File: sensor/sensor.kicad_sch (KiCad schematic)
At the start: 29 parts, among them IC1 MAX30002CWV+, IC2 LP5900TLX-2.7_NOPB, IC3 MAX86141ENP+T, J1 Conn_01x10_Female, J2 Conn_01x10_Female, J2 Probe_01_male, J3 Probe_01_male, J4 Probe_01_male, J5 Probe_01_male

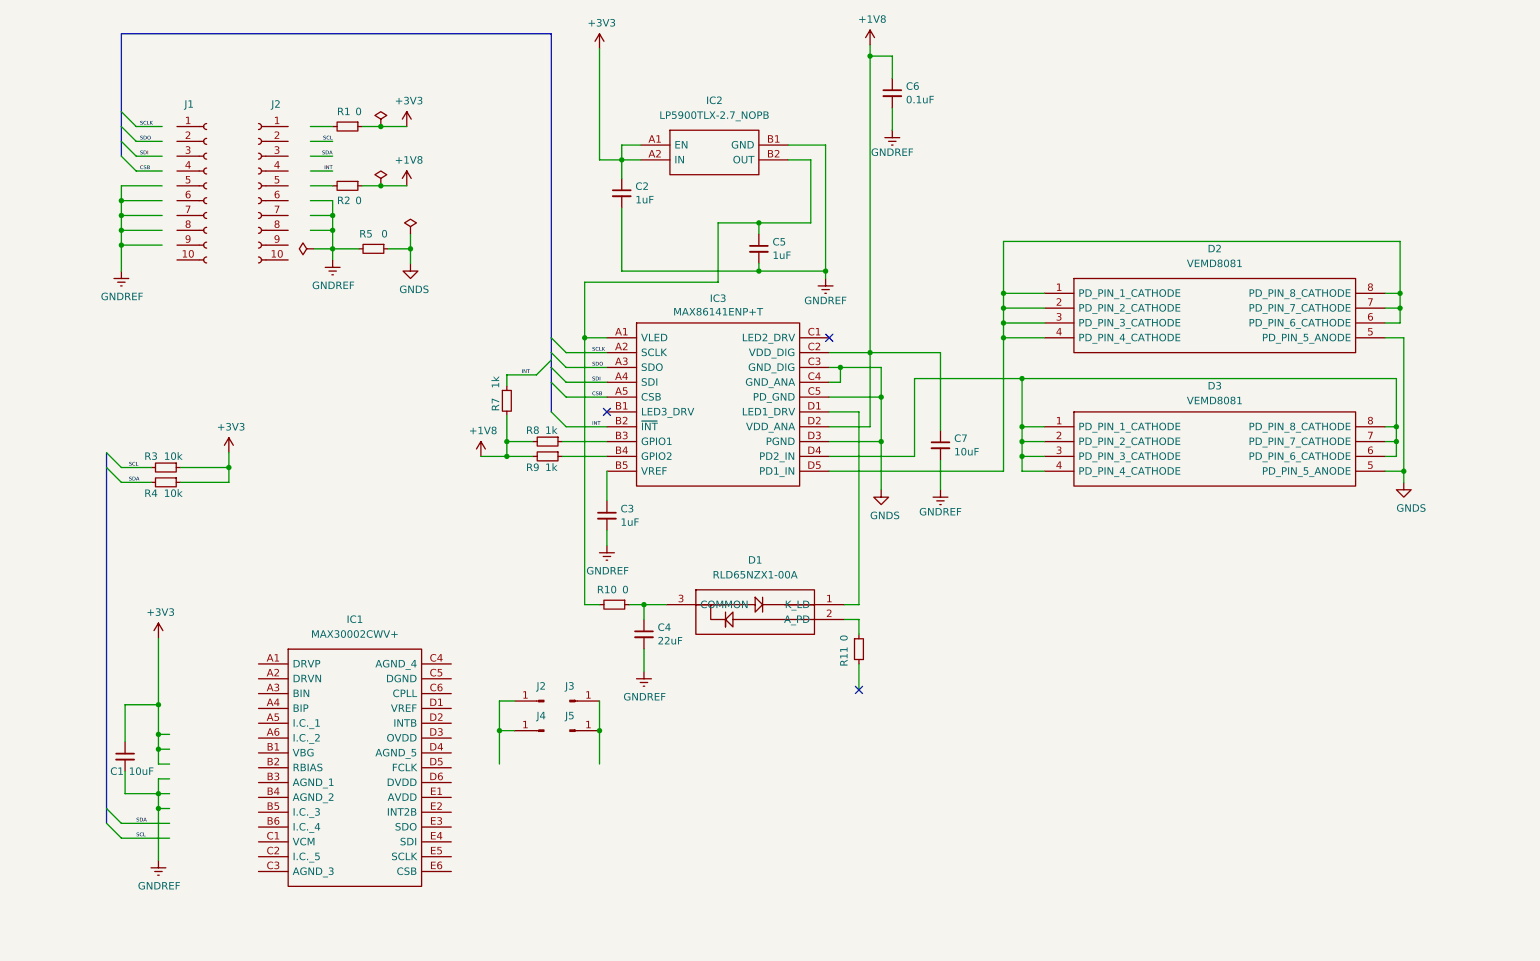
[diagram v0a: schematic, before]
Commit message: Schematic v 2.0 is ready. Can go with PCB design
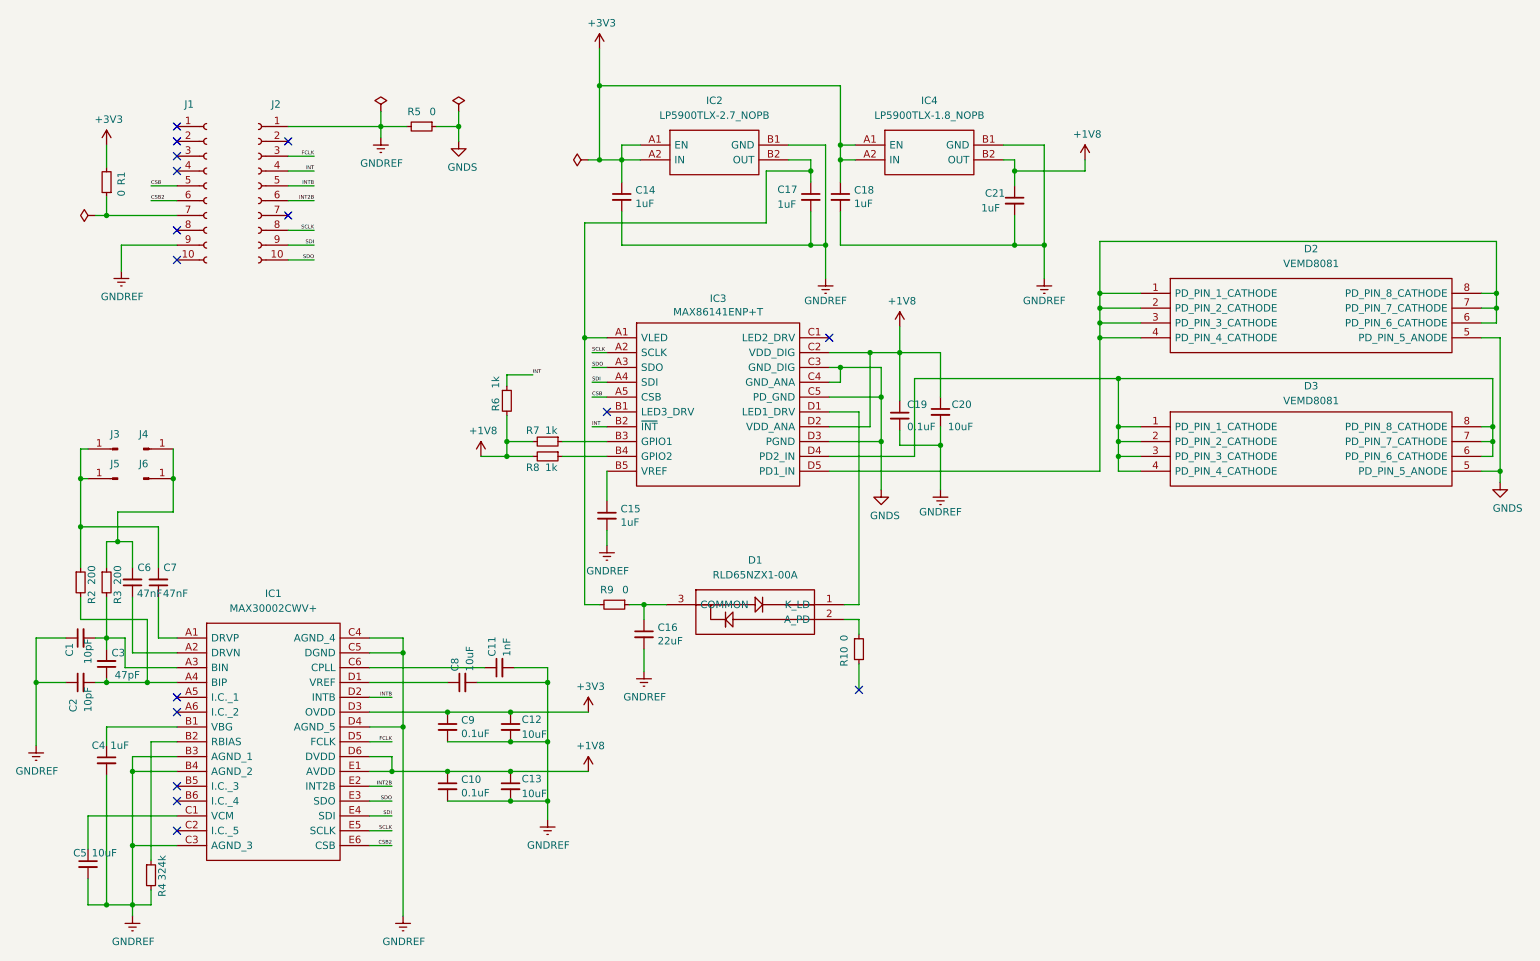
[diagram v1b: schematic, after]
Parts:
- added C1, C2: 10pF, Capacitor_SMD:C_0402_1005Metric, symbol Device:C_Small
- added C10, C9: 0.1uF, Capacitor_SMD:C_0402_1005Metric, symbol Device:C_Small
- added C11: 1nF, Capacitor_SMD:C_0402_1005Metric, symbol Device:C_Small
- added C13, C5, C8: 10uF, Capacitor_SMD:C_0402_1005Metric, symbol Device:C_Small
- added C18, C21, C4: 1uF, Capacitor_SMD:C_0402_1005Metric, symbol Device:C_Small
- added C3: 47pF, Capacitor_SMD:C_0402_1005Metric, symbol Device:C_Small
- added C6, C7: 47nF, Capacitor_SMD:C_0402_1005Metric, symbol Device:C_Small
- added IC4: LP5900TLX-1.8_NOPB, Horace:BGA4C50P2X2_105X108X68, symbol Horace:LP5900TLX-2.7_NOPB
- D1: footprint RLD85PZJ400A -> Horace:RLD85PZJ400A
- IC2: footprint BGA4C50P2X2_105X108X68 -> Horace:BGA4C50P2X2_105X108X68
- IC3: footprint BGA20C40P5X4_205X185X50 -> Horace:BGA20C40P5X4_205X185X50
- R2: value 0 -> 200; Digikey Part Number 541-4062-2-ND -> 541-3959-2-ND; Manufacturer Part Number CRCW04020000Z0EDC -> CRCW040210K0FKEDC; Mouser Price/Stock https://www.mouser.ee/ProductDetail/Vishay-Dale/CRCW0402000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 -> https://www.mouser.ee/ProductDetail/Vishay-Dale/CRCW040210K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
- R3: value 10k -> 200
- R4: value 10k -> 324k
- renumbered C1 to C12, C2 to C14, C3 to C15, C4 to C16, C5 to C17, C6 to C19, C7 to C20, J2 to J3, J3 to J4, J4 to J5, J5 to J6, R11 to R10, R7 to R6, R8 to R7, R9 to R8, R10 to R9
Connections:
- net SCL is gone; now on an unnamed net: R3.2
- net SDA is gone; now on net GNDREF: R4.2
- net +1V8: now also IC1.D6 (DVDD), IC1.E1 (AVDD), C10.1, C13.1, C21.1, IC4.B2 (OUT); no longer R2.1
- net +3V3: now also IC1.D3 (OVDD), R1.2, C18.1, C9.1, IC4.A1 (EN), IC4.A2 (IN); no longer R1.1, R3.1, R4.1
- net CSB: now also J1.5 (Pin_5)
- net GNDREF: now also IC1.B3 (AGND_1), IC1.B4 (AGND_2), IC1.C3 (AGND_3), IC1.C4 (AGND_4), IC1.C5 (DGND), IC1.D4 (AGND_5), J1.9 (Pin_9), J2.1 (Pin_1), C1.1, C10.2, C11.2, C13.2, C18.2, C2.1, C21.2, C4.2, C5.2, C8.2, C9.2, IC4.B1 (GND)
- net INT: now also J2.4 (Pin_4)
- net SCLK: now also IC1.E5 (SCLK), J2.8 (Pin_8)
- net SDI: now also IC1.E4 (SDI), J2.9 (Pin_9)
- net SDO: now also IC1.E3 (SDO), J2.10 (Pin_10)
- net at R2.2: now also IC1.A4 (BIP), C2.2, C3.1
- net at J4.1 (Pin_1), J6.1 (Pin_1): now also R3.1, C6.2
- net at J3.1 (Pin_1), J5.1 (Pin_1): now also R2.1, C7.2
- net at IC1.A1 (DRVP): now also C7.1
- net at IC1.A2 (DRVN): now also C6.1
- net at IC1.A3 (BIN): now also C1.2, C3.2
- net at IC1.B1 (VBG): now also C4.1
- net at IC1.B2 (RBIAS): now also R4.1
- net at IC1.C1 (VCM): now also C5.1
- net at IC1.C6 (CPLL): now also C11.1
- net at IC1.D1 (VREF): now also C8.1
- net INTB: now reaches IC1.D2 (INTB)
- net INTB: now also J2.5 (Pin_5)
- net FCLK: now reaches IC1.D5 (FCLK)
- net FCLK: now also J2.3 (Pin_3)
- net INT2B: now reaches IC1.E2 (INT2B)
- net INT2B: now also J2.6 (Pin_6)
- net CSB2: now reaches IC1.E6 (CSB)
- net CSB2: now also J1.6 (Pin_6)
- net at J1.7 (Pin_7): now also R1.1
- no-connect marks 3 -> 16
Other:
- moved on the sheet: C12, C14, C17, C19, C20, D2, D3, IC1, J3, J4, J5, J6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

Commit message: SIT1532AC-J5-DCC-32.768D.stp oscillator and pins re-number. Fixed board size
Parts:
- added IC4: SIT1532AC-J5-DCC-32.768D, SIT1532ACJ5DCC32768D, symbol Horace:SIT1532AC-J5-DCC-32.768D
- added R10: 0, Resistor_SMD:R_0402_1005Metric, symbol Device:R_Small
- R2, R3: Digikey Part Number 541-3959-2-ND -> 541-3995-2-ND; Manufacturer Part Number CRCW040210K0FKEDC -> CRCW0402200RFKEDC; Mouser Price/Stock https://www.mouser.ee/ProductDetail/Vishay-Dale/CRCW040210K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 -> https://www.mouser.ee/ProductDetail/Vishay-Dale/CRCW0402200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
- R4: Digikey Part Number 541-3959-2-ND -> 541-4894-2-ND; Manufacturer Part Number CRCW040210K0FKEDC -> CRCW0402324KFKEDC; Mouser Price/Stock https://www.mouser.ee/ProductDetail/Vishay-Dale/CRCW040210K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 -> https://www.mouser.ee/ProductDetail/Vishay-Dale/CRCW0402324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; Price 0.09 -> 0.2
- renumbered IC4 to IC5, R10 to R11
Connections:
- net +3V3: now also R1.1, IC4.3 (VDD); no longer R1.2
- net FCLK: now also R10.2; no longer J2.3 (Pin_3)
- net GNDREF: now also J1.10 (Pin_10), J2.2 (Pin_2), IC4.1 (GND_1), IC4.4 (GND_2); no longer J1.9 (Pin_9), J2.1 (Pin_1)
- net INT: now also J2.5 (Pin_5); no longer J2.4 (Pin_4)
- net INT2B: now also J1.8 (Pin_8); no longer J2.6 (Pin_6)
- net INTB: now also J1.7 (Pin_7); no longer J2.5 (Pin_5)
- new net: J2.4 (Pin_4), R1.2
- new net: IC4.2 (CLK_OUT), R10.1
- no-connect marks 16 -> 17
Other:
- note added: "14"
- note added: "15"
- note added: "18"
- note added: "19"
- note added: "21"
- note added: "22"
- note added: "23"
- note added: "25"
- note added: "26"
- note added: "27"
- note added: "32"
- note added: "33"
- note added: "3V3"
- note added: "4"
- note added: "5"
- note added: "5V"
- note added: "BAT"
- note added: "GND"
- note added: "RST"
- moved on the sheet: R1, R5

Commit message: Change power for oscillator. Generated annotations and updated board from schematic
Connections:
- net +1V8: now also IC4.3 (VDD)
- net +3V3: no longer IC4.3 (VDD)
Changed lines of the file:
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@@
   (junction (at 101.6 139.065) (diameter 0) (color 0 0 0 0)
+  )
+  (junction (at 114.935 149.225) (diameter 0) (color 0 0 0 0)
   )
   (junction (at 120.65 44.45) (diameter 0) (color 0 0 0 0)
@@
     (stroke (width 0) (type default) (color 0 0 0 0))
   )
-  (wire (pts (xy 120.015 149.225) (xy 120.015 153.67))
-    (stroke (width 0) (type default) (color 0 0 0 0))
-  )
   (wire (pts (xy 32.385 126.365) (xy 35.56 126.365))
     (stroke (width 0) (type default) (color 0 0 0 0))
@@
     (stroke (width 0) (type default) (color 0 0 0 0))
   )
+  (wire (pts (xy 114.935 153.67) (xy 114.935 149.225))
+    (stroke (width 0) (type default) (color 0 0 0 0))
+  )
   (wire (pts (xy 77.47 149.225) (xy 81.28 149.225))
     (stroke (width 0) (type default) (color 0 0 0 0))
@@
     (stroke (width 0) (type default) (color 0 0 0 0))
   )
+  (wire (pts (xy 114.935 146.05) (xy 114.935 149.225))
+    (stroke (width 0) (type default) (color 0 0 0 0))
+  )
   (wire (pts (xy 44.45 144.145) (xy 40.005 144.145))
     (stroke (width 0) (type default) (color 0 0 0 0))
@@
     (stroke (width 0) (type default) (color 0 0 0 0))
   )
-  (wire (pts (xy 120.015 153.67) (xy 139.065 153.67))
+  (wire (pts (xy 114.935 153.67) (xy 139.065 153.67))
     (stroke (width 0) (type default) (color 0 0 0 0))
   )
@@
     (pin "9")
   )
-  (symbol (lib_id "power:+1V8") (at 114.935 149.225 0) (unit 1)
-    (in_bom yes) (on_board yes)
-    (property "Reference" "#PWR04" (id 0) (at 114.935 153.035 0)
-      (effects (font (size 1.27 1.27)) hide)
-    )
-    (property "Value" "+1V8" (id 1) (at 115.316 144.8308 0))
-    (property "Footprint" "" (id 2) (at 114.935 149.225 0)
-      (effects (font (size 1.27 1.27)) hide)
-    )
-    (property "Datasheet" "" (id 3) (at 114.935 149.225 0)
+  (symbol (lib_id "power:+1V8") (at 114.935 146.05 0) (unit 1)
+    (in_bom yes) (on_board yes)
+    (property "Reference" "#PWR04" (id 0) (at 114.935 149.86 0)
+      (effects (font (size 1.27 1.27)) hide)
+    )
+    (property "Value" "+1V8" (id 1) (at 115.316 141.6558 0))
+    (property "Footprint" "" (id 2) (at 114.935 146.05 0)
+      (effects (font (size 1.27 1.27)) hide)
+    )
+    (property "Datasheet" "" (id 3) (at 114.935 146.05 0)
       (effects (font (size 1.27 1.27)) hide)
     )
@@
   (symbol (lib_id "power:GNDREF") (at 175.895 156.845 0) (unit 1)
     (in_bom yes) (on_board yes)
-    (property "Reference" "#PWR?" (id 0) (at 175.895 163.195 0)
+    (property "Reference" "#PWR0106" (id 0) (at 175.895 163.195 0)
       (effects (font (size 1.27 1.27)) hide)
     )
@@
     )
     (property "Datasheet" "" (id 3) (at 155.575 64.77 0)
-      (effects (font (size 1.27 1.27)) hide)
-    )
-    (pin "1")
-  )
-  (symbol (lib_id "power:+3V3") (at 120.015 149.225 0) (unit 1)
-    (in_bom yes) (on_board yes)
-    (property "Reference" "#PWR?" (id 0) (at 120.015 153.035 0)
-      (effects (font (size 1.27 1.27)) hide)
-    )
-    (property "Value" "+3V3" (id 1) (at 120.396 144.8308 0))
-    (property "Footprint" "" (id 2) (at 120.015 149.225 0)
-      (effects (font (size 1.27 1.27)) hide)
-    )
-    (property "Datasheet" "" (id 3) (at 120.015 149.225 0)
       (effects (font (size 1.27 1.27)) hide)
     )
@@
       (reference "#PWR0105") (unit 1) (value "GNDREF") (footprint "")
     )
+    (path "/b1370204-4e54-40cd-bea3-30837d0002fd"
+      (reference "#PWR0106") (unit 1) (value "GNDREF") (footprint "")
+    )
     (path "/00000000-0000-0000-0000-00005fefa4e8"
       (reference "#PWR0107") (unit 1) (value "+1V8") (footprint "")
@@
       (reference "#PWR0120") (unit 1) (value "GNDREF") (footprint "")
     )
-    (path "/b1370204-4e54-40cd-bea3-30837d0002fd"
-      (reference "#PWR?") (unit 1) (value "GNDREF") (footprint "")
-    )
-    (path "/c76b22ac-4a66-4dd6-8c50-28270f0bafce"
-      (reference "#PWR?") (unit 1) (value "+3V3") (footprint "")
-    )
     (path "/8016a108-4510-42c5-a56d-49096fa3f052"

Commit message: BOM check complete
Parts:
- removed R1: 0, Resistor_SMD:R_0402_1005Metric, symbol Device:R_Small
- C1, C2: Digikey Part Number 311-1729-2-ND -> 311-3777-2-ND; Manufacturer Part Number CC0402MRX5R5BB106 -> CC0402KRNPO7BN100; Price 0.22 -> 0.1
- C11: Digikey Part Number 311-1729-2-ND -> 13-CC0402JRNPO7BN102TR-ND; Manufacturer Part Number CC0402MRX5R5BB106 -> CC0402JRNPO7BN102
- C16: value 22uF -> 10uF; Digikey Part Number 311-3479-2-ND -> 311-1729-2-ND; Manufacturer Part Number CC0402MRX5R5BB226 -> CC0402MRX5R5BB106; Mouser Price/Stock https://www.mouser.ee/ProductDetail/Yageo/CC0402MRX5R5BB226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 -> https://www.mouser.ee/ProductDetail/Yageo/CC0402MRX5R5BB106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; Price 0.38 -> 0.22
- C3: Digikey Part Number 311-1729-2-ND -> 311-3751-2-ND; Manufacturer Part Number CC0402MRX5R5BB106 -> CC0402JRNPO8BN470
- C6, C7: Digikey Part Number 311-1729-2-ND -> 311-1688-2-ND; Manufacturer Part Number CC0402MRX5R5BB106 -> CC0402KRX5R6BB473
- IC1: Digikey Part Number (none) -> MAX30002CWV+-ND
- IC4: value SIT1532AC-J5-DCC-32.768D -> SIT1532AC
- renumbered R2 to R1, R11 to R10, R3 to R2, R4 to R3, R5 to R4, R6 to R5, R7 to R6, R8 to R7, R9 to R8, R10 to R9
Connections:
- net +3V3: now also J2.4 (Pin_4)

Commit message: new parts alignment based on SPI bus connections
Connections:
- net CSB: now also J2.5 (Pin_5); no longer J1.5 (Pin_5)
- net CSB2: now also J1.8 (Pin_8); no longer J1.6 (Pin_6)
- net INT: now also J2.8 (Pin_8); no longer J2.5 (Pin_5)
- net INT2B: now also J2.10 (Pin_10); no longer J1.8 (Pin_8)
- net INTB: now also J2.9 (Pin_9); no longer J1.7 (Pin_7)
- net SCLK: now also J1.7 (Pin_7); no longer J2.8 (Pin_8)
- net SDI: now also J1.6 (Pin_6); no longer J2.9 (Pin_9)
- net SDO: now also J1.5 (Pin_5); no longer J2.10 (Pin_10)
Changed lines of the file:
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@@
     (effects (font (size 0.635 0.635)) (justify right bottom))
   )
-  (label "CSB2" (at 40.005 51.435 0)
+  (label "CSB2" (at 40.005 56.515 0)
     (effects (font (size 0.635 0.635)) (justify left bottom))
   )
-  (label "SCLK" (at 67.945 56.515 180)
+  (label "SCLK" (at 40.005 53.975 0)
+    (effects (font (size 0.635 0.635)) (justify left bottom))
+  )
+  (label "INTB" (at 67.945 59.055 180)
     (effects (font (size 0.635 0.635)) (justify right bottom))
   )
-  (label "INTB" (at 40.005 53.975 0)
-    (effects (font (size 0.635 0.635)) (justify left bottom))
-  )
-  (label "INT2B" (at 40.005 56.515 0)
-    (effects (font (size 0.635 0.635)) (justify left bottom))
+  (label "INT2B" (at 67.945 61.595 180)
+    (effects (font (size 0.635 0.635)) (justify right bottom))
   )
   (label "SCLK" (at 115.57 77.47 0)
     (effects (font (size 0.635 0.635)) (justify left bottom))
   )
-  (label "INT" (at 67.945 48.895 180)
+  (label "INT" (at 67.945 56.515 180)
     (effects (font (size 0.635 0.635)) (justify right bottom))
   )
@@
     (effects (font (size 0.635 0.635)) (justify right bottom))
   )
-  (label "SDO" (at 67.945 61.595 180)
-    (effects (font (size 0.635 0.635)) (justify right bottom))
+  (label "SDO" (at 40.005 48.895 0)
+    (effects (font (size 0.635 0.635)) (justify left bottom))
   )
   (label "INT2B" (at 81.28 151.765 180)
     (effects (font (size 0.635 0.635)) (justify right bottom))
   )
-  (label "SDI" (at 67.945 59.055 180)
-    (effects (font (size 0.635 0.635)) (justify right bottom))
+  (label "SDI" (at 40.005 51.435 0)
+    (effects (font (size 0.635 0.635)) (justify left bottom))
   )
   (label "INTB" (at 81.28 136.525 180)
     (effects (font (size 0.635 0.635)) (justify right bottom))
   )
-  (label "CSB" (at 40.005 48.895 0)
-    (effects (font (size 0.635 0.635)) (justify left bottom))
+  (label "CSB" (at 67.945 48.895 180)
+    (effects (font (size 0.635 0.635)) (justify right bottom))
   )
   (label "SDO" (at 115.57 80.01 0)

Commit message: all elements are placed on the board
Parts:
- removed R10: 0, Resistor_SMD:R_0402_1005Metric, symbol Device:R_Small
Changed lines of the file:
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@@
   (no_connect (at 156.21 74.93))
   (no_connect (at 63.5 38.735))
-  (no_connect (at 161.29 135.255))
+  (no_connect (at 158.75 123.19))
   (no_connect (at 44.45 139.065))
   (no_connect (at 44.45 151.765))
@@
     (stroke (width 0) (type default) (color 0 0 0 0))
   )
-  (wire (pts (xy 161.29 123.19) (xy 161.29 125.73))
-    (stroke (width 0) (type default) (color 0 0 0 0))
-  )
   (wire (pts (xy 168.275 93.345) (xy 175.26 93.345))
     (stroke (width 0) (type default) (color 0 0 0 0))
@@
     (stroke (width 0) (type default) (color 0 0 0 0))
   )
-  (wire (pts (xy 158.75 123.19) (xy 161.29 123.19))
-    (stroke (width 0) (type default) (color 0 0 0 0))
-  )
   (wire (pts (xy 77.47 149.225) (xy 81.28 149.225))
     (stroke (width 0) (type default) (color 0 0 0 0))
@@
     (stroke (width 0) (type default) (color 0 0 0 0))
   )
-  (wire (pts (xy 161.29 130.81) (xy 161.29 135.255))
-    (stroke (width 0) (type default) (color 0 0 0 0))
-  )
   (wire (pts (xy 124.46 128.27) (xy 124.46 132.08))
     (stroke (width 0) (type default) (color 0 0 0 0))
@@
     (pin "2")
   )
-  (symbol (lib_id "Device:R_Small") (at 161.29 128.27 0) (unit 1)
-    (in_bom yes) (on_board yes)
-    (property "Reference" "R10" (id 0) (at 158.75 129.54 90))
-    (property "Value" "0" (id 1) (at 158.75 126.365 90))
-    (property "Footprint" "Resistor_SMD:R_0402_1005Metric" (id 2) (at 161.29 128.27 0)
-      (effects (font (size 1.27 1.27)) hide)
-    )
-    (property "Datasheet" "https://www.mouser.ee/datasheet/2/427/crcwce3-1762584.pdf" (id 3) (at 161.29 128.27 0)
-      (effects (font (size 1.27 1.27)) hide)
-    )
-    (property "Manufacturer" "Vishay / Dale" (id 4) (at 161.29 128.27 90)
-      (effects (font (size 1.27 1.27)) hide)
-    )
-    (property "Manufacturer Part Number" "CRCW04020000Z0EDC" (id 5) (at 161.29 128.27 90)
-      (effects (font (size 1.27 1.27)) hide)
-    )
-    (property "Mouser Price/Stock" "https://www.mouser.ee/ProductDetail/Vishay-Dale/CRCW04020000Z0EDC/?qs=sGAEpiMZZMvdGkrng054t0DrEhLhGh8gwkqbMx2gSI%252BmKUnjnIW1MQ%3D%3D" (id 6) (at 161.29 128.27 90)
-      (effects (font (size 1.27 1.27)) hide)
-    )
-    (property "Digikey Part Number" "541-4062-2-ND" (id 7) (at 161.29 128.27 90)
-      (effects (font (size 1.27 1.27)) hide)
-    )
-    (property "Price" "0.09" (id 8) (at 161.29 128.27 90)
-      (effects (font (size 1.27 1.27)) hide)
-    )
-    (pin "1")
-    (pin "2")
-  )
   (symbol (lib_id "Device:C_Small") (at 153.035 50.8 0) (unit 1)
     (in_bom yes) (on_board yes)
@@
       (reference "R9") (unit 1) (value "0") (footprint "Resistor_SMD:R_0402_1005Metric")
     )
-    (path "/e34b9d89-aa5b-4d91-ab61-aa20f80172ef"
-      (reference "R10") (unit 1) (value "0") (footprint "Resistor_SMD:R_0402_1005Metric")
-    )
   )

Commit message: more wires, only one left
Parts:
- IC4: footprint SIT1532ACJ5DCC32768D -> Horace:SIT1532ACJ5DCC32768D
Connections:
- net INT2B: now also J2.9 (Pin_9); no longer J2.10 (Pin_10)
- net INTB: now also J2.10 (Pin_10); no longer J2.9 (Pin_9)
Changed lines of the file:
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@@
     (effects (font (size 0.635 0.635)) (justify left bottom))
   )
-  (label "INTB" (at 67.945 59.055 180)
+  (label "INTB" (at 67.945 61.595 180)
     (effects (font (size 0.635 0.635)) (justify right bottom))
   )
-  (label "INT2B" (at 67.945 61.595 180)
+  (label "INT2B" (at 67.945 59.055 180)
     (effects (font (size 0.635 0.635)) (justify right bottom))
   )
@@
     (property "Reference" "IC4" (id 0) (at 155.575 143.51 0))
     (property "Value" "SIT1532AC" (id 1) (at 155.575 146.05 0))
-    (property "Footprint" "SIT1532ACJ5DCC32768D" (id 2) (at 142.875 156.21 0)
+    (property "Footprint" "Horace:SIT1532ACJ5DCC32768D" (id 2) (at 142.875 156.21 0)
       (effects (font (size 1.27 1.27)) (justify left) hide)
     )
@@
     )
     (path "/ae288591-2b20-4235-9845-5e99a9d6c0fe"
-      (reference "IC4") (unit 1) (value "SIT1532AC") (footprint "SIT1532ACJ5DCC32768D")
+      (reference "IC4") (unit 1) (value "SIT1532AC") (footprint "Horace:SIT1532ACJ5DCC32768D")
     )
     (path "/74bd9dab-0398-4fa6-aad9-5469b650bfac"
